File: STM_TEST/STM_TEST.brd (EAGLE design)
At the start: 59.9 x 69.6 mm, 53 parts, among them U1 TPS2115APWR, U2 AZ1117EH-3.3TRG1, Y1 ECS-80-S-4X, Y2 ECS-80-S-4X

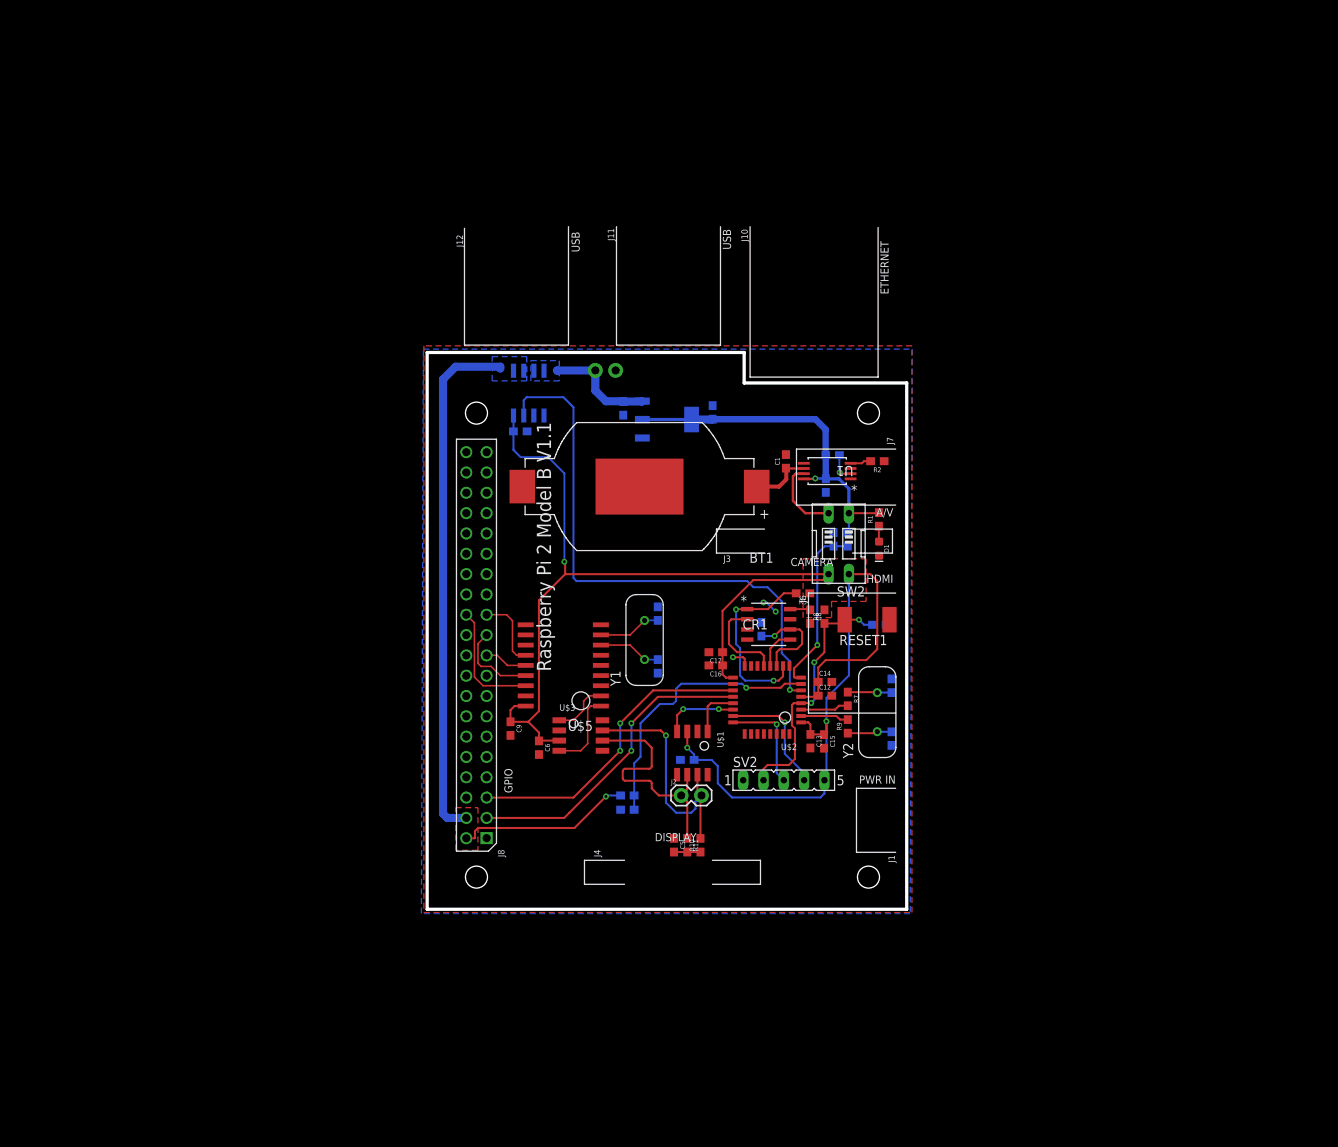
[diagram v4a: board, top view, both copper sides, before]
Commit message: Added some gnd vias
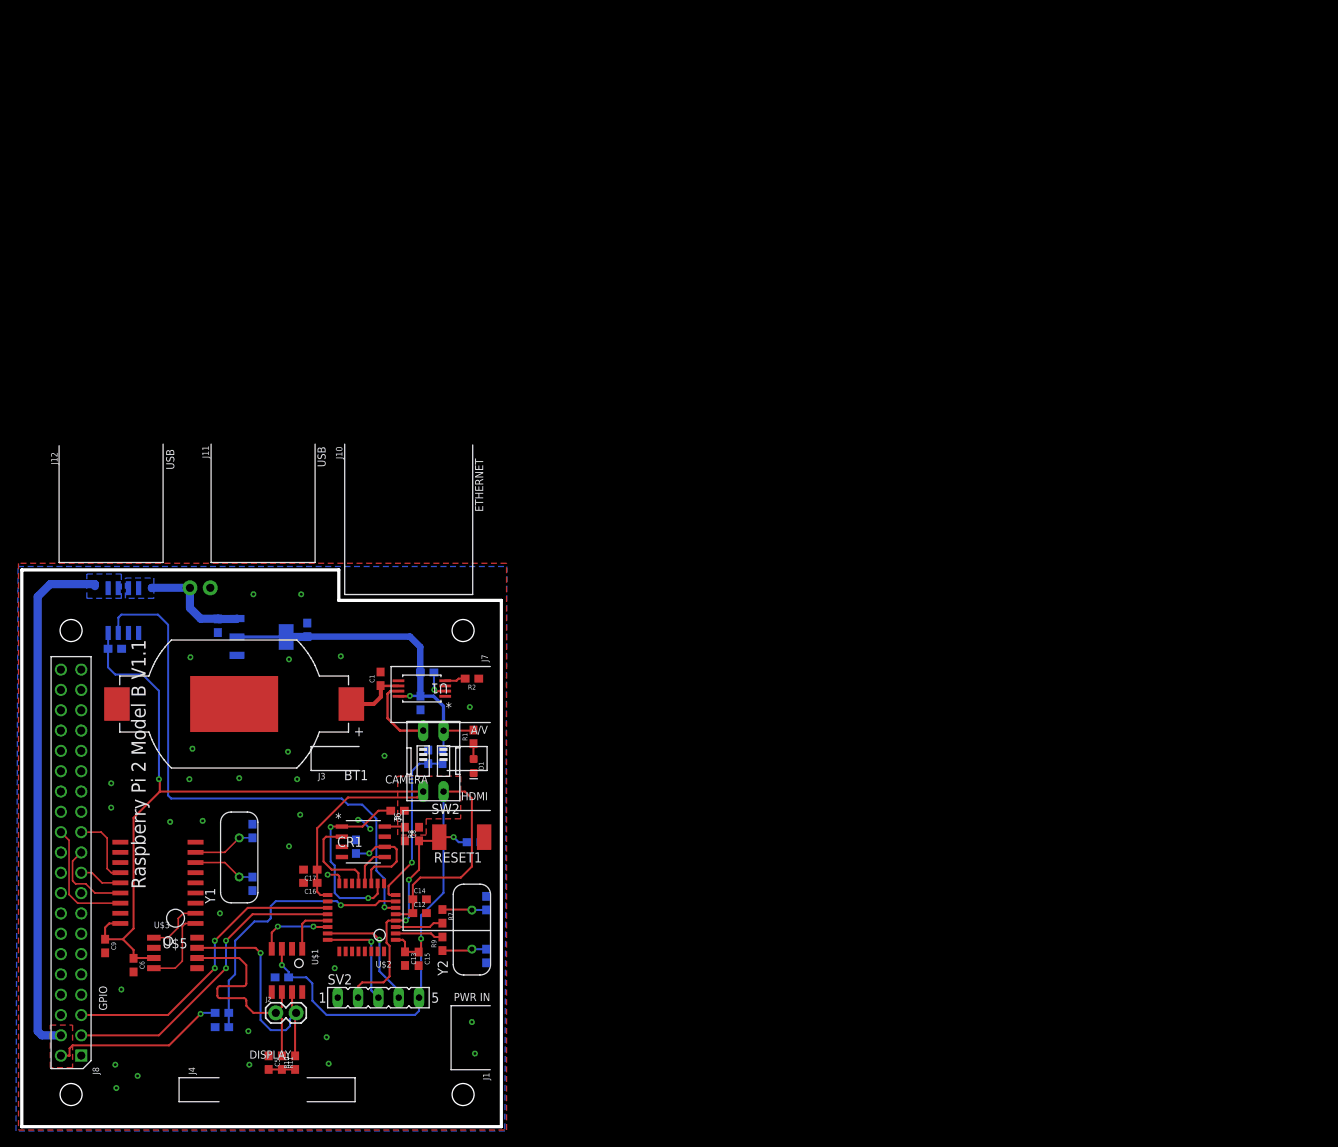
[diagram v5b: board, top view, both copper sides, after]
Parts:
- moved C8 57.5 mm to (48.3, 36.8)
- moved D1 57.5 mm to (56.9, 45.3)
- moved U$2 57.5 mm to (47.1, 29.2)
- moved U1 57.5 mm to (50.4, 55.0)
- moved C1 57.5 mm to (45.2, 56.2)
- moved C10 57.5 mm to (56.9, 35.8)
- moved C12 57.5 mm to (50.1, 26.9)
- moved C14 57.5 mm to (50.1, 28.7)
- moved C15 57.5 mm to (50.0, 21.2)
- moved C16 57.5 mm to (36.4, 30.7)
- moved C17 57.5 mm to (36.4, 32.4)
- moved C19 57.5 mm to (58.4, 21.6)
- moved C2 57.5 mm to (50.2, 53.2)
- moved C20 57.5 mm to (58.4, 28.2)
- moved C21 57.5 mm to (36.1, 62.4)
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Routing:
- net GND: vias 3 -> 33
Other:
- board text added: "Data_Logger_rev1 Designed By: Jacob Bobson Sam Deghuee Jason King"
